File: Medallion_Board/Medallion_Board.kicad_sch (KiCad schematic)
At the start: 84 parts, among them IC1 Wio-SX1262, J1 SWD HEADER, J2 EXPANSION, J3 IPEX, P1 JST_BTN_1, P2 JST_BTN_2, P3 JST_BTN_3, Q1 DMG3415U, U1 MDBT50Q-1MV2, U2 MAX17048G_T10, U3 LC86LICMD, U4 RT9080-33GJ5, U5 MCP73831T-2ACI_OT, U6 BNO085, X1 USB4085-GF-A, Y1 32.768KHZ

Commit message: Some notes. Figuring out costs
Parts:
- C1, C10, C11, C12, C13, C14, C15, C16, C17, C18, C19, C2, C20, C21, C22, C23, C24, C25, C26, C27, C28, C3, C4, C5, C6, C7, C9, R1, R10, R11, R12, R13, R14, R15, R16, R17, R18, R19, R2, R20, R21, R3, R4, R5, R6, R7, R8, R9: PRICE (none) -> 0.07
- C29, C30: MPN 0805W106K6R3CC -> (none); now not fitted
- D10, D11, D3, D4, D5, D6, D7, D8, D9: PRICE (none) -> 0.10
- D12: Availability In Stock -> (none); Check_prices https://www.snapeda.com/parts/TPD1E05U06DPYR/Texas+Instrume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 -> (none); MPN (none) -> TPD1E05U06DPYR; PRICE (none) -> 0.29; Package X1SON-2 Texas Instruments -> (none); Price None -> (none); SnapEDA_Link https://www.snapeda.com/parts/TPD1E05U06DPYR/Texas+Instrume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 -> (none)
- J3: MPN (none) -> RECE.20369.001E.01; PRICE (none) -> 0.77

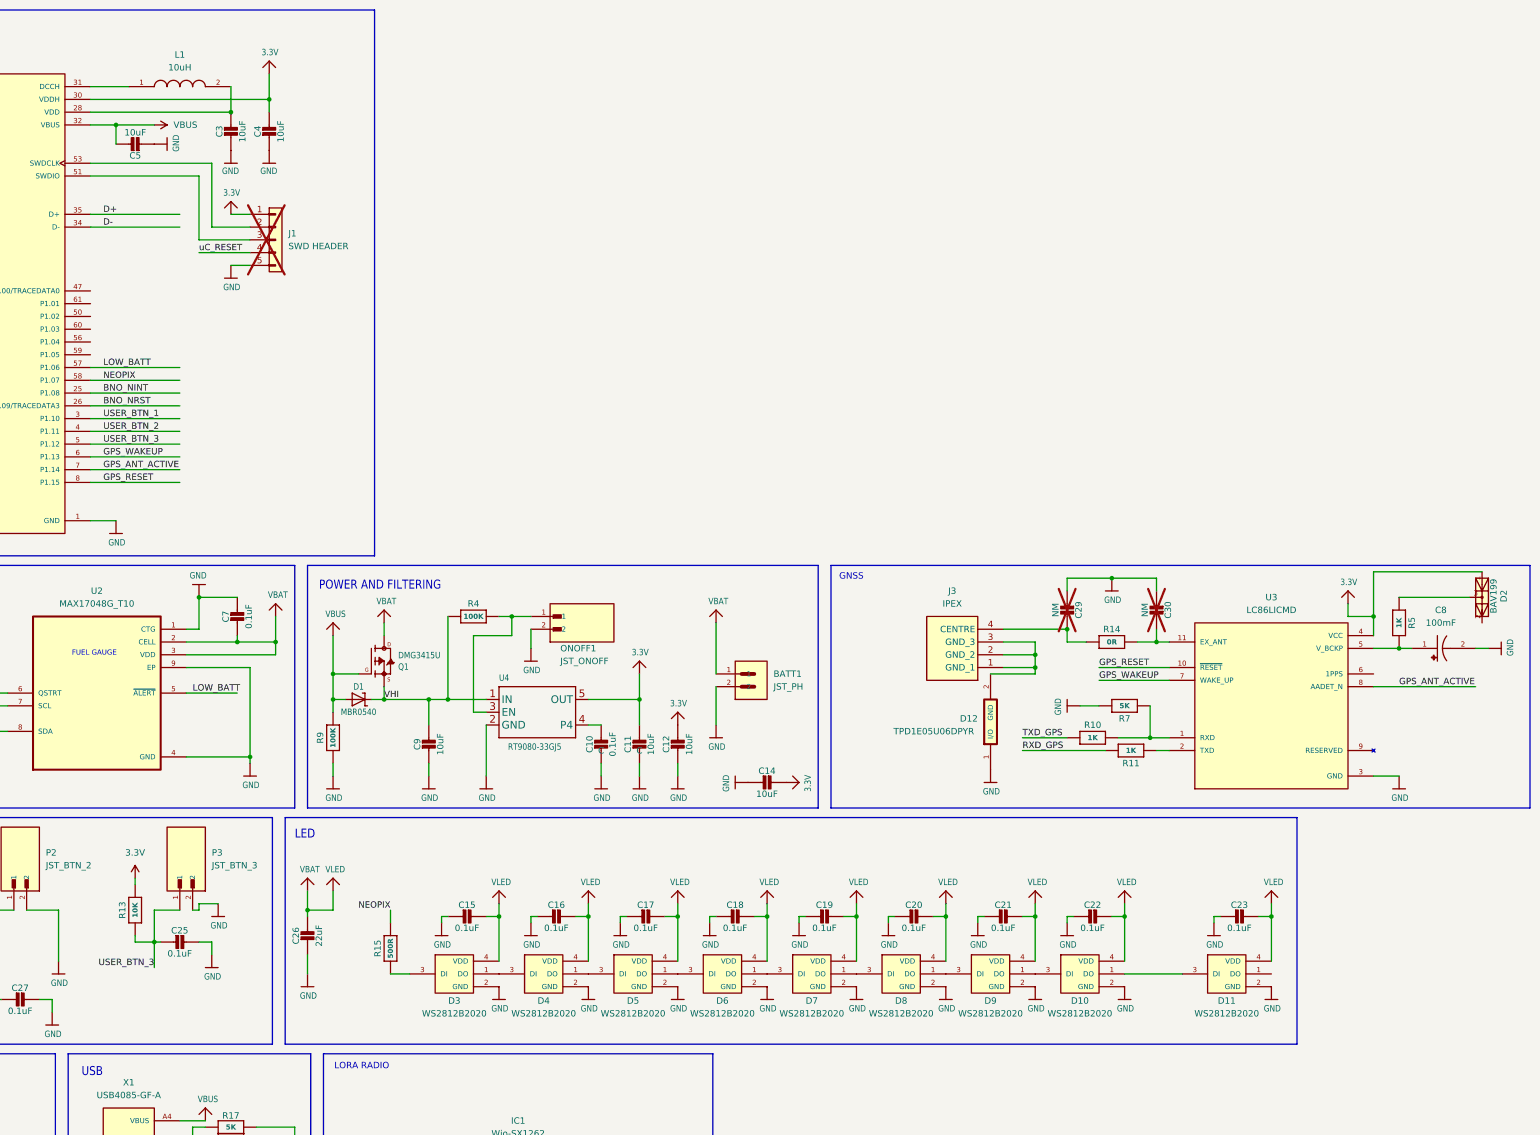
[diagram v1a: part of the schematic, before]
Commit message: Wrote some more readme stuff. Added haptics to the schematic
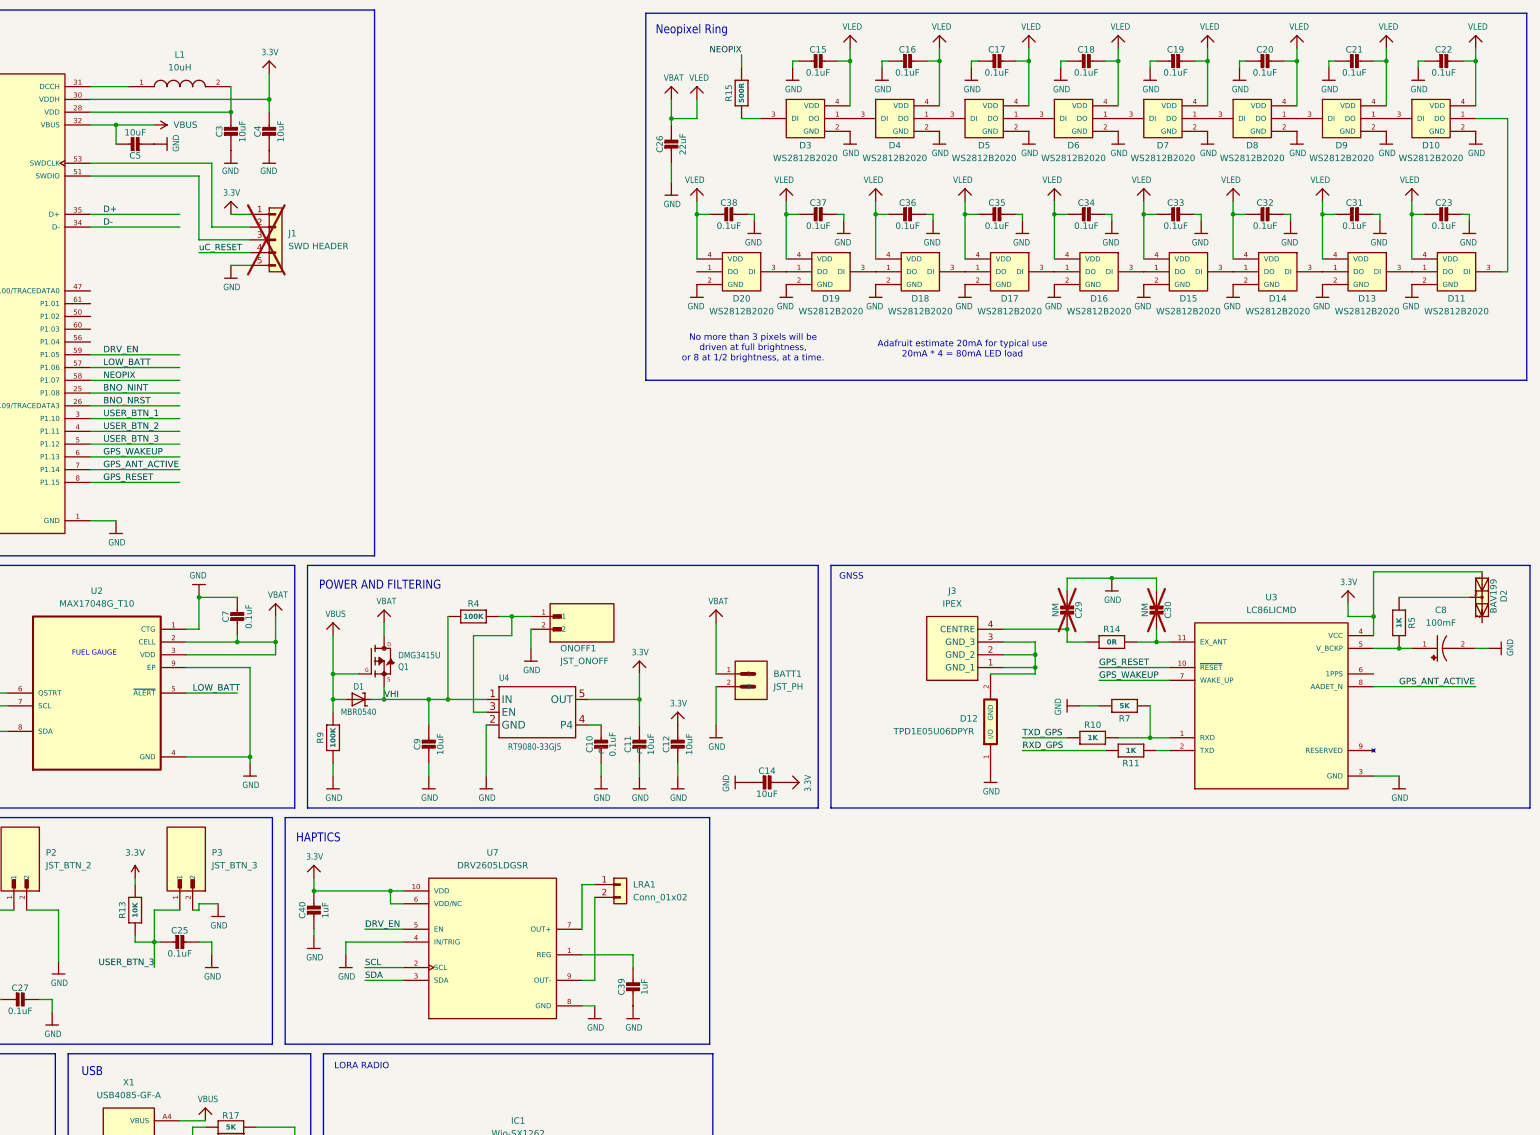
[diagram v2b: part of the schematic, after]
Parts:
- added C31, C32, C33, C34, C35, C36, C37, C38: 0.1uF, Capacitor_SMD:C_0402_1005Metric, symbol Adafruit ESP32-S3 8MB No PSRAM-eagle-import:CAP_CERAMIC0805-NOOUTLINE
- added C39, C40: 1uF, Capacitor_SMD:C_0603_1608Metric, symbol Adafruit ESP32-S3 8MB No PSRAM-eagle-import:CAP_CERAMIC0603_NO
- added D13, D14, D15, D16, D17, D18, D19, D20: WS2812B2020, WS2812B2020:LED_WS2812B2020, symbol WS2812B2020:WS2812B2020
- added LRA1: Conn_01x02, Connector_PinHeader_2.54mm:PinHeader_1x02_P2.54mm_Vertical, symbol Connector_Generic:Conn_01x02
- added U7: DRV2605LDGSR, DRV2605LDGSR:SOP50P490X110-10N, symbol DRV2605LDGSR:DRV2605LDGSR
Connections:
- net 3.3V: now also C40.1, U7.10 (VDD), U7.6 (VDD/NC)
- net GND: now also C31.2, C32.2, C33.2, C34.2, C35.2, C36.2, C37.2, C38.2, C39.2, C40.2, D13.2 (GND), D14.2 (GND), D15.2 (GND), D16.2 (GND), D17.2 (GND), D18.2 (GND), D19.2 (GND), D20.2 (GND), U7.4 (IN/TRIG), U7.8 (GND)
- net SCL: now also U7.2 (SCL)
- net SDA: now also U7.3 (SDA)
- net VBAT: now also C31.1, C32.1, C33.1, C34.1, C35.1, C36.1, C37.1, C38.1, D13.4 (VDD), D14.4 (VDD), D15.4 (VDD), D16.4 (VDD), D17.4 (VDD), D18.4 (VDD), D19.4 (VDD), D20.4 (VDD)
- net DRV_EN: now reaches U1.59 (P1.05)
- net DRV_EN: now also U7.5 (EN)
- net at D11.1 (DO): now also D13.3 (DI)
- new net: D15.1 (DO), D16.3 (DI)
- new net: D14.1 (DO), D15.3 (DI)
- new net: D16.1 (DO), D17.3 (DI)
- new net: D19.1 (DO), D20.3 (DI)
- new net: C39.1, U7.1 (REG)
- new net: D18.1 (DO), D19.3 (DI)
- new net: D17.1 (DO), D18.3 (DI)
- new net: LRA1.1 (Pin_1), U7.7 (OUT+)
- new net: LRA1.2 (Pin_2), U7.9 (OUT-)
- new net: D13.1 (DO), D14.3 (DI)
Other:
- note added: "Adafruit estimate 20mA for typical use 20mA * 4 = 80mA LED load"
- note added: "HAPTICS"
- note added: "Neopixel Ring"
- note added: "No more than 3 pixels will be driven at full brightness, or 8 at 1/2 brightness, at a time."
- note removed: "LED"
- moved on the sheet: C15, C16, C17, C18, C19, C20, C21, C22, C26, D10, D3, D4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

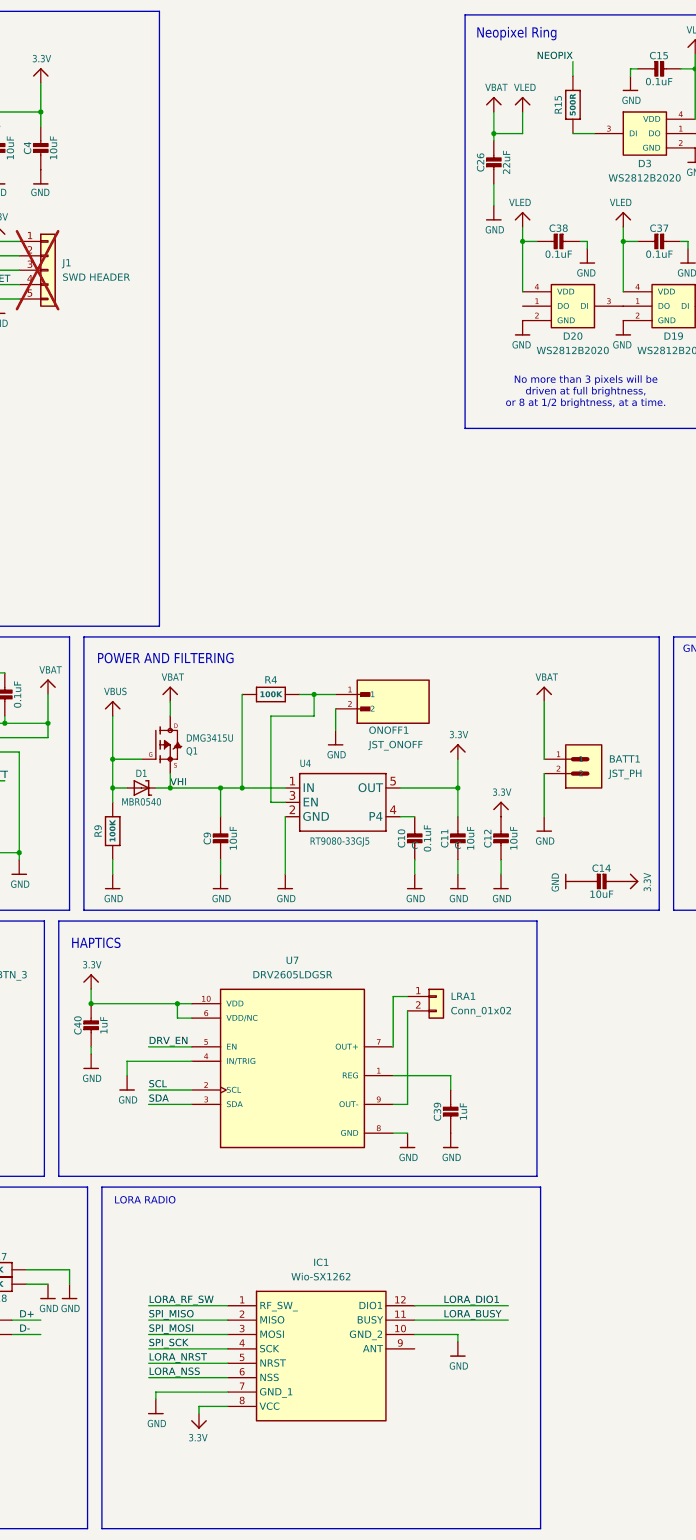
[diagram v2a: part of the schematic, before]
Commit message: Update the board components, and assign footprints and BOM stuff to haptics
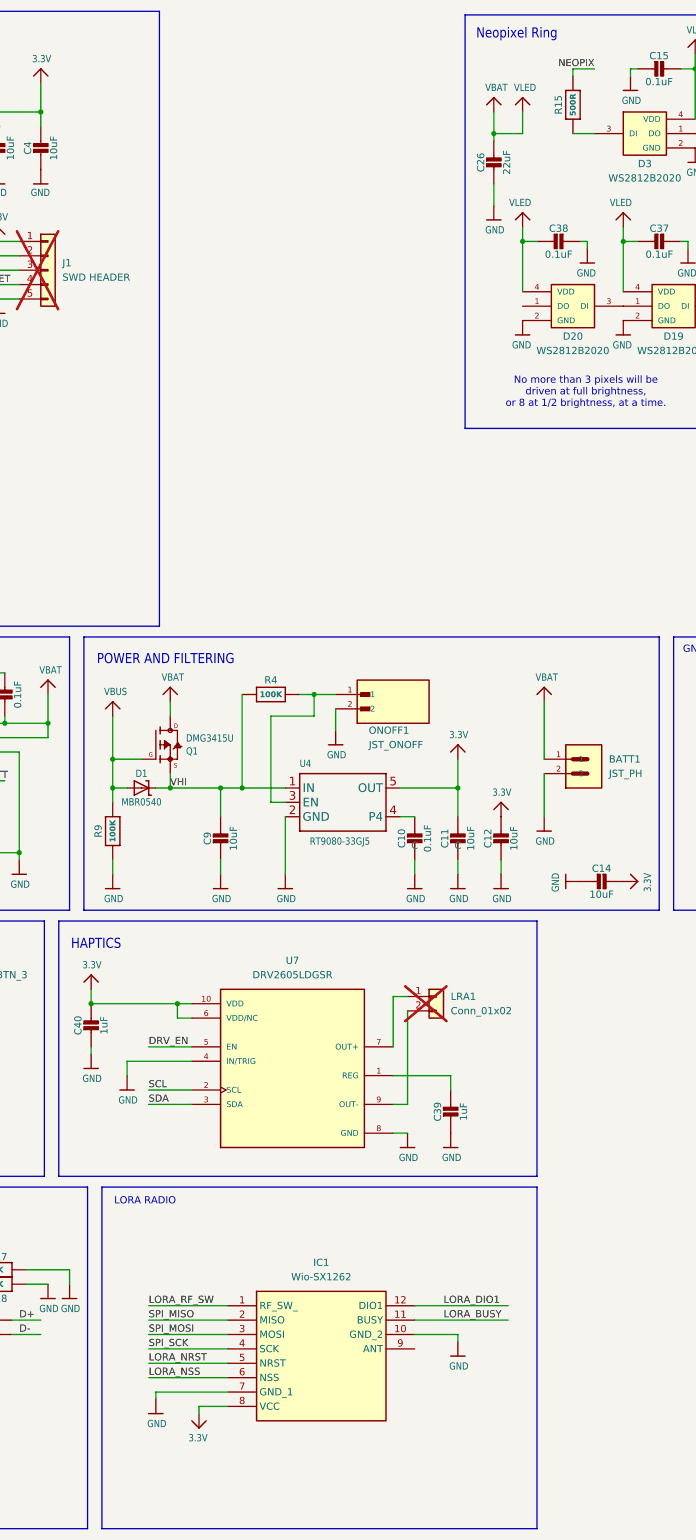
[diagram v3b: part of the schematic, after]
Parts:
- LRA1: MPN (none) -> VG1040003D; PRICE (none) -> 4.47; now not fitted
- U7: Availability In Stock -> (none); Check_prices https://www.snapeda.com/parts/DRV2605LDGSR/Texas+Instrument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 -> (none); MPN (none) -> DRV2605LDGSR; PRICE (none) -> 1.69; Package VSSOP-10 Texas Instruments -> (none); Price None -> (none); SnapEDA_Link https://www.snapeda.com/parts/DRV2605LDGSR/Texas+Instrument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 -> (none)
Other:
- title: Off-grid People Tracking Puck -> Smart Compass
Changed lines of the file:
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@@
 	(paper "A3")
 	(title_block
-		(title "Off-grid People Tracking Puck")
-		(date "2026-05-29")
+		(title "Smart Compass")
+		(date "2026-06-02")
 	)

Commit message: Added flash memory
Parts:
- added C41: 0.1uF, Capacitor_SMD:C_0402_1005Metric, symbol Adafruit ESP32-S3 8MB No PSRAM-eagle-import:CAP_CERAMIC0805-NOOUTLINE
- added R22: 10K, Resistor_SMD:R_0603_1608Metric, symbol Adafruit ESP32-S3 8MB No PSRAM-eagle-import:RESISTOR_0603_NOOUT
- added U8: MX25R6435FZAIH0, MX25R6435FZAIH0:SON80P400X400X60-9N, symbol MX25R6435FZAIH0:MX25R6435FZAIH0
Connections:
- net 3.3V: now also C41.1, R22.2, U8.8 (VCC)
- net GND: now also C41.2, U8.4 (GND)
- net SPI_MISO: now also U8.2 (SO/SIO1)
- net SPI_MOSI: now also U8.5 (SI/SIO0)
- net SPI_SCK: now also U8.6 (SCLK)
- new net FLASH_CS: R22.1, U8.1 (CS#)
- new net FLASH_RST: U8.7 (RESET#/SIO3)
- new net FLASH_WP: U8.3 (WP#/SIO2)
- no-connect marks 0 -> 12
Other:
- note added: "FLASH"
- note added: "From the datasheet Section 12: Please note that a pull-up resistor on CS# may ensure a safe and proper power-up/down level."
- note added: "Unused but implemented just in case"
- note added: "V_BCKP enables much faster location acquisition 30s -> 2s"
- moved on the sheet: BATT1, C12, C14, C29, C30, C8, D12, D2, IC1, J3, R10, R11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

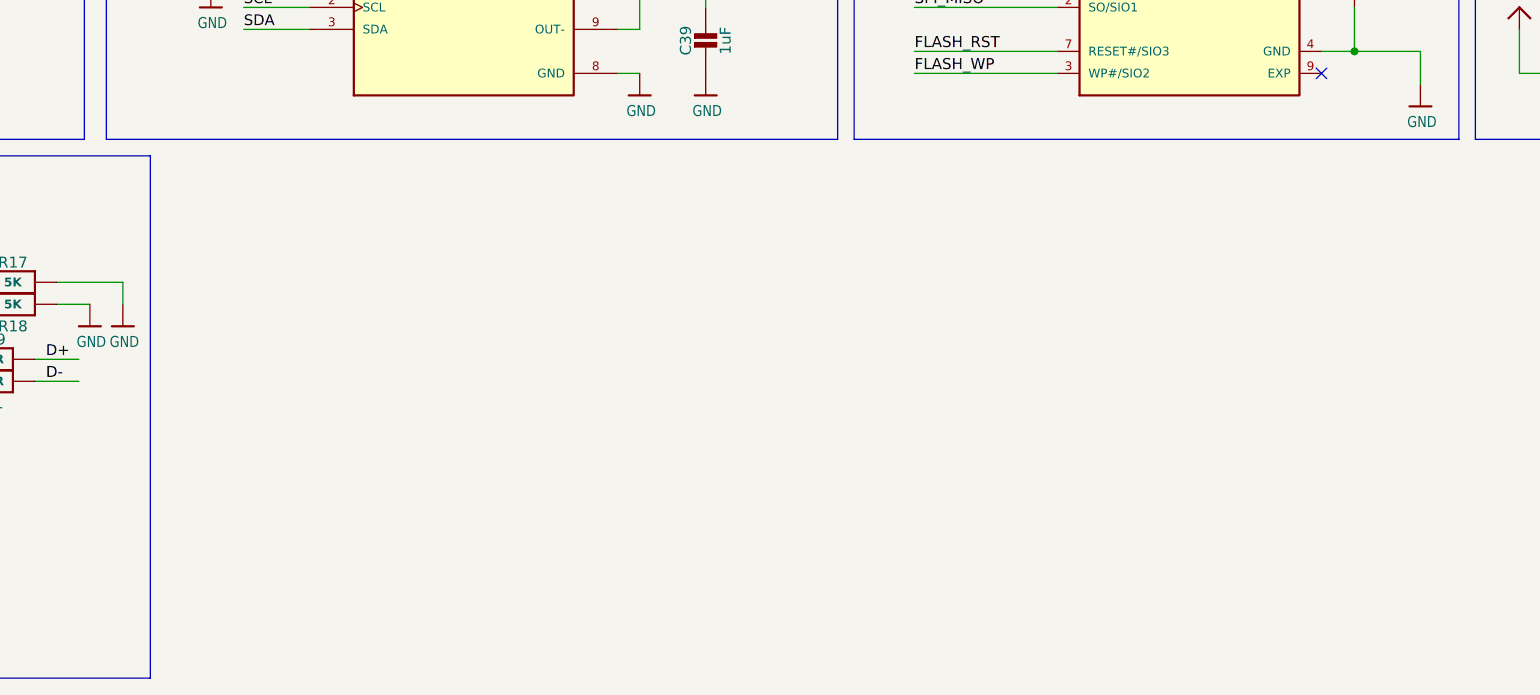
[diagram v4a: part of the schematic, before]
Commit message: wire up the eink connector
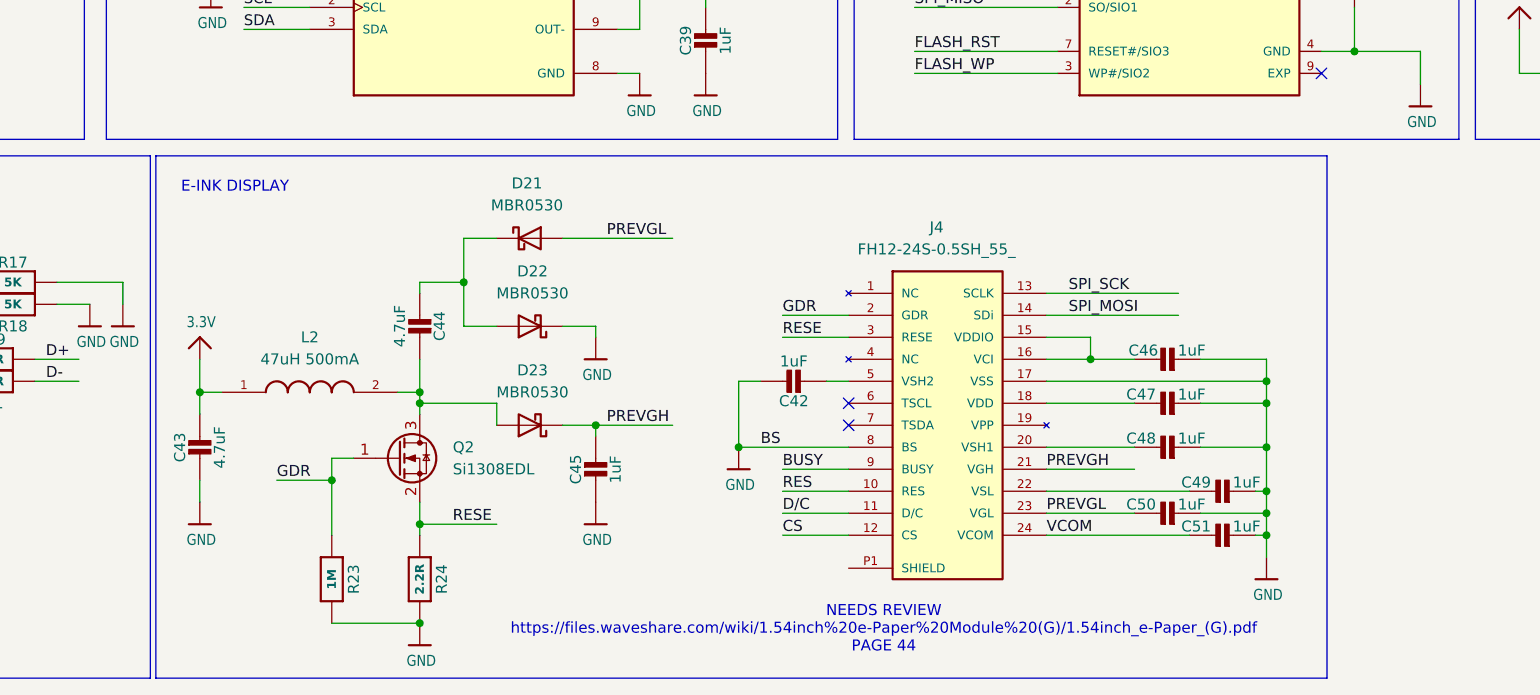
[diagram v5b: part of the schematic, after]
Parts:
- added C42, C45, C46, C47, C48, C49, C50, C51: 1uF, Capacitor_SMD:C_0603_1608Metric, symbol Adafruit ESP32-S3 8MB No PSRAM-eagle-import:CAP_CERAMIC0603_NO
- added C43, C44: 4.7uF, Capacitor_SMD:C_0603_1608Metric, symbol Adafruit ESP32-S3 8MB No PSRAM-eagle-import:CAP_CERAMIC0603_NO
- added D21, D22, D23: MBR0530, Diode_SMD:D_SOD-123, symbol Diode:MBR0530
- added J4: FH12-24S-0.5SH_55_, FH12-24S-0.5SH_55_:HRS_FH12-24S-0.5SH_55_, symbol FH12-24S-0.5SH_55_:FH12-24S-0.5SH_55_
- added L2: 47uH 500mA, symbol LQM18DN100M70L:LQM18DN100M70L
- added Q2: Si1308EDL, Package_TO_SOT_SMD:SOT-323_SC-70, symbol Transistor_FET:Si1308EDL
- added R23: 1M, Resistor_SMD:R_0603_1608Metric, symbol Adafruit ESP32-S3 8MB No PSRAM-eagle-import:RESISTOR_0603_NOOUT
- added R24: 2.2R, Resistor_SMD:R_0603_1608Metric, symbol Adafruit ESP32-S3 8MB No PSRAM-eagle-import:RESISTOR_0603_NOOUT
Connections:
- net 3.3V: now also C43.1, L2.1
- net GND: now also C42.1, C43.2, C45.2, C46.2, C47.2, C48.2, C49.2, C50.2, C51.2, D22.1 (K), J4.17 (VSS), J4.8 (BS), R23.2, R24.2
- net SPI_MOSI: now also J4.14 (SDi)
- net SPI_SCK: now also J4.13 (SCLK)
- new net: C44.1, D23.2 (A), L2.2, Q2.3 (D)
- new net: C46.1, J4.15 (VDDIO), J4.16 (VCI)
- new net: C44.2, D21.1 (K), D22.2 (A)
- new net: C47.1, J4.18 (VDD)
- new net: C49.1, J4.22 (VSL)
- new net: C48.1, J4.20 (VSH1)
- new net: C42.2, J4.5 (VSH2)
- new net BUSY: J4.9 (BUSY)
- new net CS: J4.12 (CS)
- new net D/C: J4.11 (D/C)
- new net GDR: J4.2 (GDR), Q2.1 (G), R23.1
- new net PREVGH: C45.1, D23.1 (K), J4.21 (VGH)
- new net PREVGL: C50.1, D21.2 (A), J4.23 (VGL)
- new net RES: J4.10 (RES)
- new net RESE: J4.3 (RESE), Q2.2 (S), R24.1
- new net VCOM: C51.1, J4.24 (VCOM)
- no-connect marks 12 -> 14
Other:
- note added: "E-INK DISPLAY"
- note added: "NEEDS REVIEW https://files.waveshare.com/wiki/1.54inch%20e-Paper%20Module%20(G)/1.54inch_e-Paper_(G).pdf PAGE 44"
